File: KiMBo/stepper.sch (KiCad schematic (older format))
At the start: 18 parts

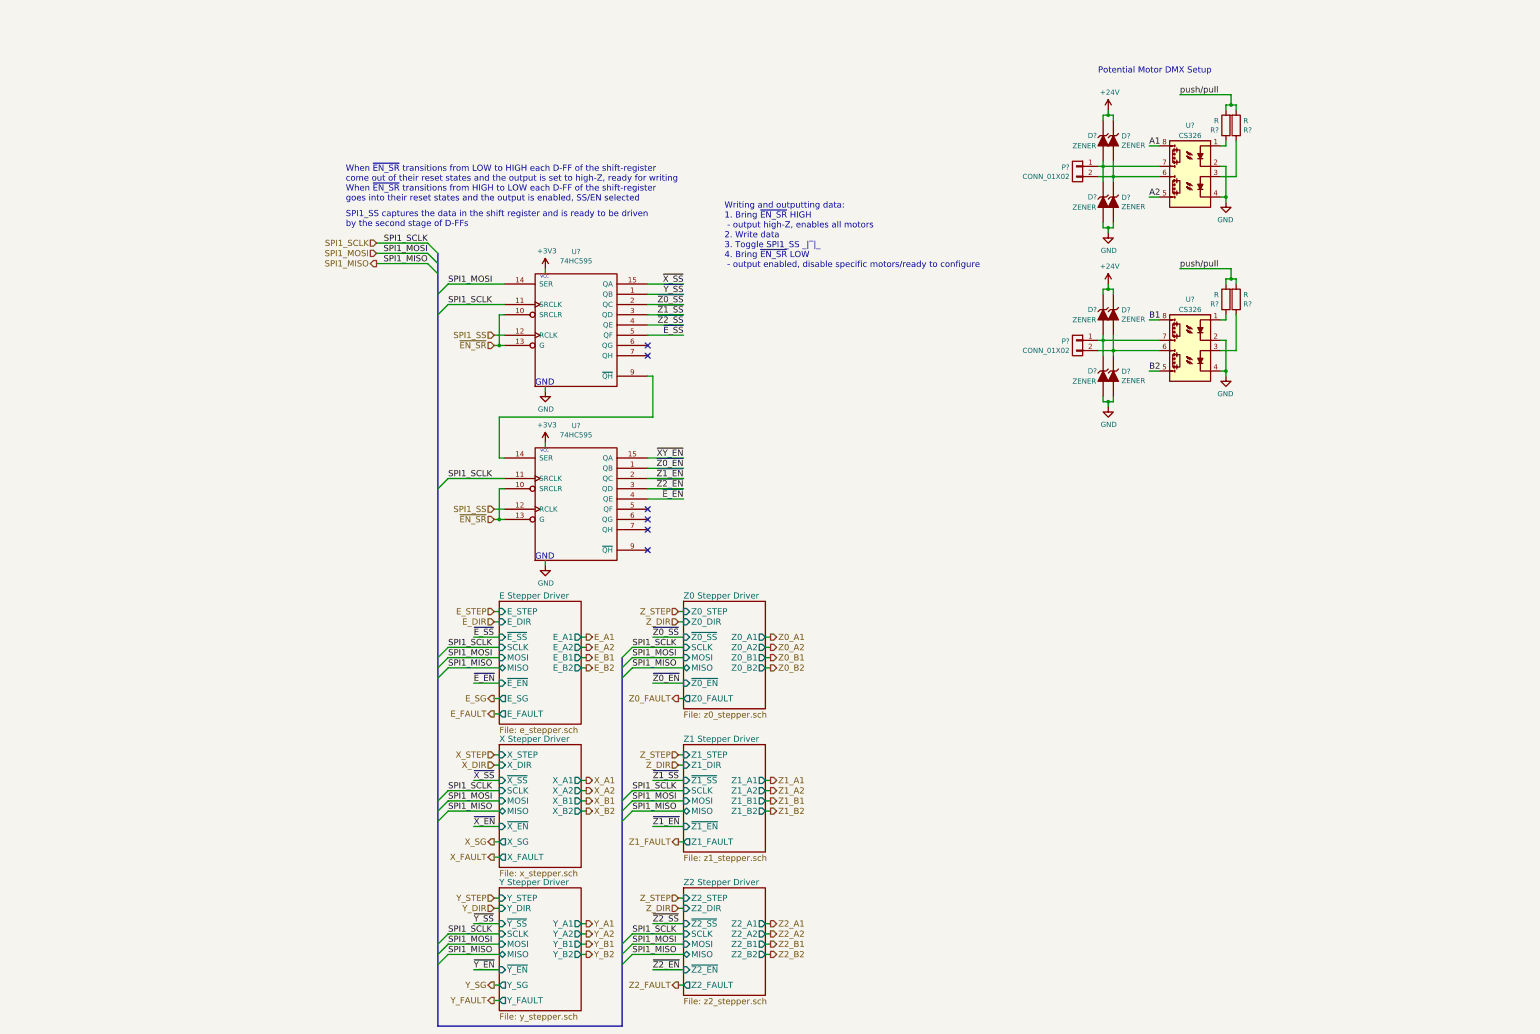
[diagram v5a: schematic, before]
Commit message: Create nodes for more SS, add H stepper, begin fixing power rail names
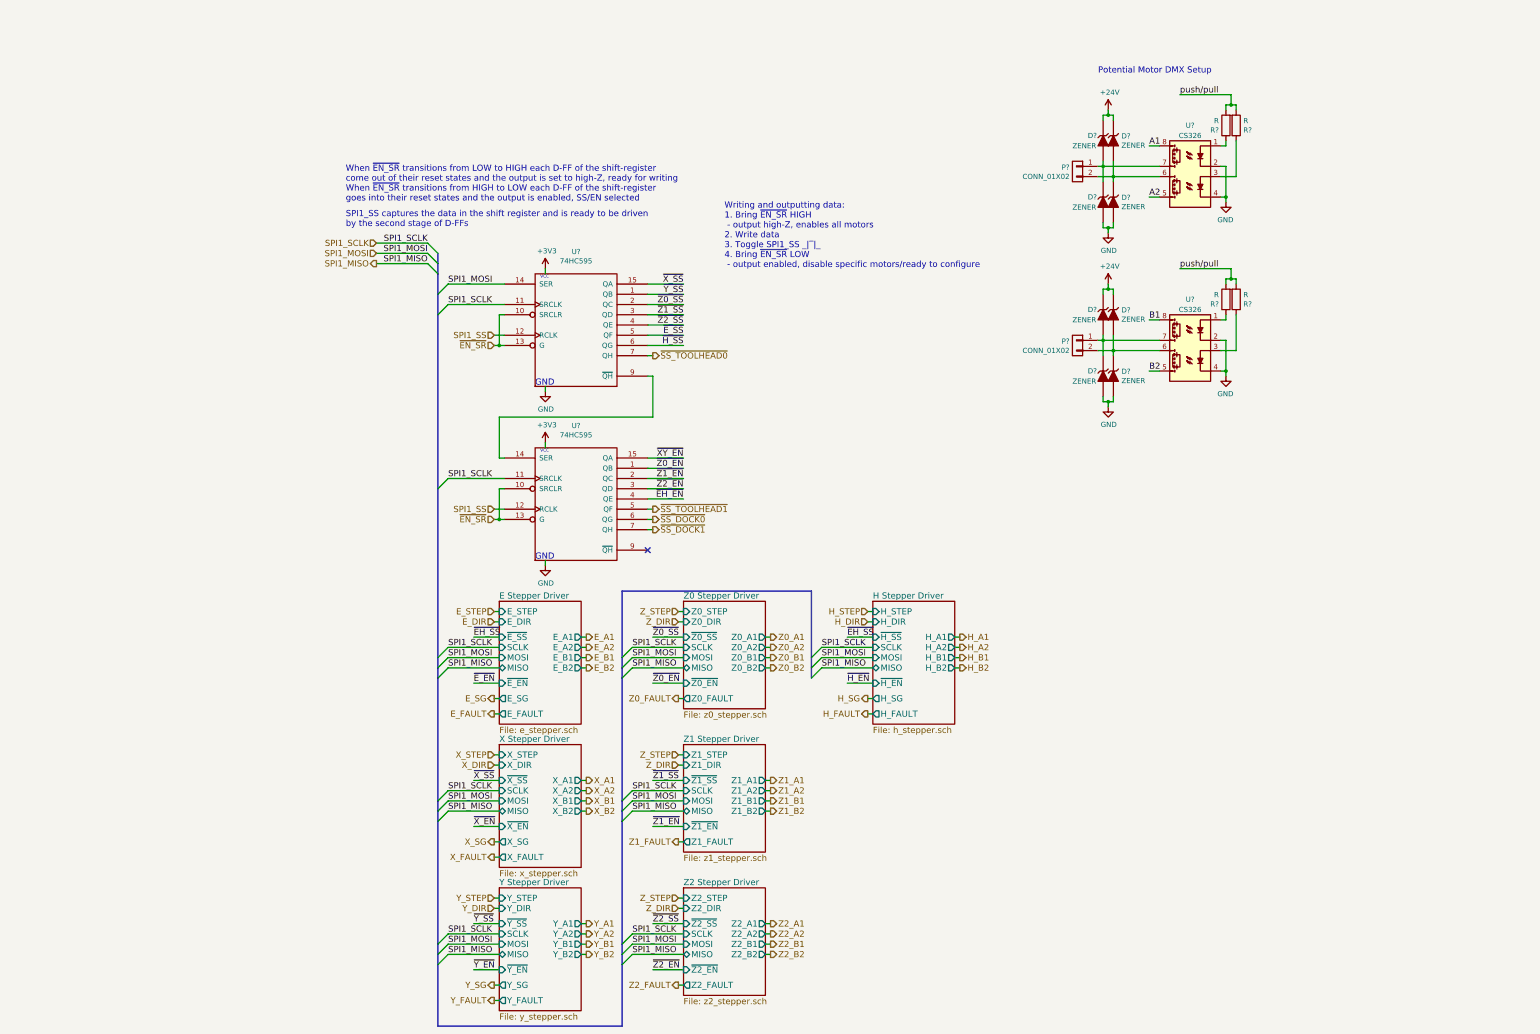
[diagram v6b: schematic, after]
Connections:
- net ~E_EN: no longer U?.4 (QE)
- net ~H_SS: now reaches U?.6 (QG)
- net ~SS_TOOLHEAD0: now reaches U?.7 (QH)
- net ~SS_TOOLHEAD1: now reaches U?.5 (QF)
- net ~SS_DOCK0: now reaches U?.6 (QG)
- net ~SS_DOCK1: now reaches U?.7 (QH)
- new net ~EH_EN: U?.4 (QE)
- no-connect marks 6 -> 1
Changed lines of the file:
@@
 $Descr A3 16535 11693
 encoding utf-8
-Sheet 16 23
+Sheet 10 25
 Title ""
 Date ""
@@
 ~Z2_SS
 Text Label 7200 5350 2    60   ~ 0
-~E_EN
+~EH_EN
 Text Label 7200 4950 2    60   ~ 0
 ~XY_EN
@@
 VCC
 Text Label 5150 6700 0    60   ~ 0
-~E_SS
+~EH_SS
 Text HLabel 5350 3850 0    60   Input ~ 0
 ~EN_SR
@@
 	4900 3450 5450 3450
 Wire Wire Line
-	5350 3850 5450 3850
+	5350 3850 5400 3850
+Wire Wire Line
+	5400 3850 5450 3850
 Wire Wire Line
 	5450 3750 5350 3750
@@
 Connection ~ 11400 3900
 Wire Wire Line
-	11400 3750 11400 3950
+	11400 3750 11400 3900
+Wire Wire Line
+	11400 3900 11400 3950
 Connection ~ 11300 3800
 Wire Wire Line
-	11300 3750 11300 3950
+	11300 3750 11300 3800
+Wire Wire Line
+	11300 3800 11300 3950
 Connection ~ 11350 4400
 Wire Wire Line
 	11350 4450 11350 4400
 Wire Wire Line
-	11300 4400 11400 4400
+	11300 4400 11350 4400
+Wire Wire Line
+	11350 4400 11400 4400
 Wire Wire Line
 	11400 4400 11400 4350
@@
 	11350 3300 11350 3250
 Wire Wire Line
-	11300 3300 11400 3300
+	11300 3300 11350 3300
+Wire Wire Line
+	11350 3300 11400 3300
 Wire Wire Line
 	11400 3300 11400 3350
@@
 	11850 3600 11750 3600
 Wire Wire Line
-	11250 3800 11850 3800
-Wire Wire Line
-	11250 3900 11850 3900
+	11250 3800 11300 3800
+Wire Wire Line
+	11300 3800 11850 3800
+Wire Wire Line
+	11250 3900 11400 3900
+Wire Wire Line
+	11400 3900 11850 3900
 Wire Wire Line
 	12550 3100 12050 3100
@@
 Connection ~ 12550 3200
 Wire Wire Line
-	12500 3200 12600 3200
+	12500 3200 12550 3200
+Wire Wire Line
+	12550 3200 12600 3200
 Wire Wire Line
 	12600 3200 12600 3250
@@
 	12500 3200 12500 3250
 Wire Wire Line
-	12500 3800 12500 4150
+	12500 3800 12500 4100
+Wire Wire Line
+	12500 4100 12500 4150
 Wire Wire Line
 	12450 4100 12500 4100
@@
 Connection ~ 11400 2200
 Wire Wire Line
-	11400 2050 11400 2250
+	11400 2050 11400 2200
+Wire Wire Line
+	11400 2200 11400 2250
 Connection ~ 11300 2100
 Wire Wire Line
-	11300 2050 11300 2250
+	11300 2050 11300 2100
+Wire Wire Line
+	11300 2100 11300 2250
 Connection ~ 11350 2700
 Wire Wire Line
 	11350 2750 11350 2700
 Wire Wire Line
-	11300 2700 11400 2700
+	11300 2700 11350 2700
+Wire Wire Line
+	11350 2700 11400 2700
 Wire Wire Line
 	11400 2700 11400 2650
@@
 	11350 1600 11350 1550
 Wire Wire Line
-	11300 1600 11400 1600
+	11300 1600 11350 1600
+Wire Wire Line
+	11350 1600 11400 1600
 Wire Wire Line
 	11400 1600 11400 1650
@@
 	11850 1900 11750 1900
 Wire Wire Line
-	11250 2100 11850 2100
-Wire Wire Line
-	11250 2200 11850 2200
+	11250 2100 11300 2100
+Wire Wire Line
+	11300 2100 11850 2100
+Wire Wire Line
+	11250 2200 11400 2200
+Wire Wire Line
+	11400 2200 11850 2200
 Wire Wire Line
 	12550 1400 12050 1400
@@
 Connection ~ 12550 1500
 Wire Wire Line
-	12500 1500 12600 1500
+	12500 1500 12550 1500
+Wire Wire Line
+	12550 1500 12600 1500
 Wire Wire Line
 	12600 1500 12600 1550
@@
 	12500 1500 12500 1550
 Wire Wire Line
-	12500 2100 12500 2450
+	12500 2100 12500 2400
+Wire Wire Line
+	12500 2400 12500 2450
 Wire Wire Line
 	12450 2400 12500 2400
@@
 	5400 6450 5350 6450
 Wire Bus Line
-	4800 2950 4800 10500
+	4800 2950 4800 3050
+Wire Bus Line
+	4800 3050 4800 3150
+Wire Bus Line
+	4800 3150 4800 3350
+Wire Bus Line
+	4800 3350 4800 3550
+Wire Bus Line
+	4800 3550 4800 5250
+Wire Bus Line
+	4800 5250 4800 6900
+Wire Bus Line
+	4800 6900 4800 7000
+Wire Bus Line
+	4800 7000 4800 7100
+Wire Bus Line
+	4800 7100 4800 8300
+Wire Bus Line
+	4800 8300 4800 8400
+Wire Bus Line
+	4800 8400 4800 8500
+Wire Bus Line
+	4800 8500 4800 9700
+Wire Bus Line
+	4800 9700 4800 9800
+Wire Bus Line
+	4800 9800 4800 9900
+Wire Bus Line
+	4800 9900 4800 10500
 Wire Wire Line
 	4900 7000 5400 7000
@@
 	4900 6800 5400 6800
 Wire Bus Line
-	6600 6900 6600 10500
+	6600 6250 6600 6900
+Wire Bus Line
+	6600 6900 6600 7000
+Wire Bus Line
+	6600 7000 6600 7100
+Wire Bus Line
+	6600 7100 6600 8300
+Wire Bus Line
+	6600 8300 6600 8400
+Wire Bus Line
+	6600 8400 6600 8500
+Wire Bus Line
+	6600 8500 6600 9700
+Wire Bus Line
+	6600 9700 6600 9800
+Wire Bus Line
+	6600 9800 6600 9900
+Wire Bus Line
+	6600 9900 6600 10500
 Wire Bus Line
 	6600 10500 4800 10500
@@
 	4900 5150 5450 5150
 Wire Wire Line
-	5350 5550 5450 5550
+	5350 5550 5400 5550
+Wire Wire Line
+	5400 5550 5450 5550
 Wire Wire Line
 	5450 5450 5350 5450
@@
 Text Label 7200 5250 2    60   ~ 0
 ~Z2_EN
-NoConn ~ 6850 5450
-NoConn ~ 6850 5550
-NoConn ~ 6850 5650
-NoConn ~ 6850 3850
 Wire Wire Line
 	5450 4950 5400 4950
@@
 Text Notes 7600 3100 0    60   ~ 0
 Writing and outputting data:\n1. Bring ~EN_SR~ HIGH\n - output high-Z, enables all motors\n2. Write data\n3. Toggle SPI1_SS _|‾|_\n4. Bring ~EN_SR~ LOW\n - output enabled, disable specific motors/ready to configure
-NoConn ~ 6850 3950
 Entry Wire Line
 	4900 5150 4800 5250
@@
 F13 "~Z2_EN" I L 7200 9950 60
 $EndSheet
+$Sheet
+S 9050 6350 800  1200
+U 59A0BA3D
+F0 "H Stepper Driver" 60
+F1 "h_stepper.sch" 60
+F2 "SCLK" I L 9050 6800 60
+F3 "MISO" T L 9050 7000 60
+F4 "MOSI" I L 9050 6900 60
+F5 "H_A1" O R 9850 6700 60
+F6 "H_A2" O R 9850 6800 60
+F7 "H_B1" O R 9850 6900 60
+F8 "H_B2" O R 9850 7000 60
+F9 "H_STEP" I L 9050 6450 60
+F10 "H_DIR" I L 9050 6550 60
+F11 "~H_SS" I L 9050 6700 60
+F12 "~H_EN" I L 9050 7150 60
+F13 "H_SG" O L 9050 7300 60
+F14 "H_FAULT" O L 9050 7450 60
+$EndSheet
+Entry Wire Line
+	8550 7000 8450 7100
+Entry Wire Line
+	8550 6900 8450 7000
+Text HLabel 9000 6450 0    60   Input ~ 0
+H_STEP
+Text HLabel 9000 6550 0    60   Input ~ 0
+H_DIR
+Text HLabel 9000 7300 0    60   Output ~ 0
+H_SG
+Text Label 8800 6700 0    60   ~ 0
+~EH_SS
+Text Label 8800 7150 0    60   ~ 0
+~H_EN
+Entry Wire Line
+	8550 6800 8450 6900
+Text Label 8550 6900 0    60   ~ 0
+SPI1_MOSI
+Text Label 8550 6800 0    60   ~ 0
+SPI1_SCLK
+Text Label 8550 7000 0    60   ~ 0
+SPI1_MISO
+Wire Wire Line
+	9050 7300 9000 7300
+Wire Wire Line
+	9050 7150 8800 7150
+Wire Wire Line
+	9050 6700 8800 6700
+Wire Wire Line
+	9050 6550 9000 6550
+Wire Wire Line
+	9050 6450 9000 6450
+Wire Wire Line
+	8550 7000 9050 7000
+Wire Wire Line
+	8550 6900 9050 6900
+Wire Wire Line
+	8550 6800 9050 6800
+Wire Wire Line
+	9850 6700 9900 6700
+Wire Wire Line
+	9850 6800 9900 6800
+Wire Wire Line
+	9850 6900 9900 6900
+Wire Wire Line
+	9850 7000 9900 7000
+Text HLabel 9000 7450 0    60   Output ~ 0
+H_FAULT
+Wire Wire Line
+	9050 7450 9000 7450
+Text HLabel 9900 6700 2    60   Output ~ 0
+H_A1
+Text HLabel 9900 6800 2    60   Output ~ 0
+H_A2
+Text HLabel 9900 6900 2    60   Output ~ 0
+H_B1
+Text HLabel 9900 7000 2    60   Output ~ 0
+H_B2
+Wire Bus Line
+	8450 6250 8450 6900
+Wire Bus Line
+	8450 6900 8450 7000
+Wire Bus Line
+	8450 7000 8450 7100
+Wire Bus Line
+	8450 6250 6600 6250
+Wire Wire Line
+	6850 5450 6900 5450
+Wire Wire Line
+	6850 3850 7200 3850
+Text Label 7200 3850 2    60   ~ 0
+~H_SS
+Text HLabel 6900 3950 2    60   Output ~ 0
+~SS_TOOLHEAD0
+Wire Wire Line
+	6850 3950 6900 3950
+Text HLabel 6900 5550 2    60   Output ~ 0
+~SS_DOCK0
+Text HLabel 6900 5650 2    60   Output ~ 0
+~SS_DOCK1
+Wire Wire Line
+	6850 5550 6900 5550
+Wire Wire Line
+	6850 5650 6900 5650
+Text HLabel 6900 5450 2    60   Output ~ 0
+~SS_TOOLHEAD1
 $EndSCHEMATC

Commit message: Update the rest of the power rails and add two more stepper drivers
Now has *nine* stepper drivers, this will increase cost, and may drastically increase development time...
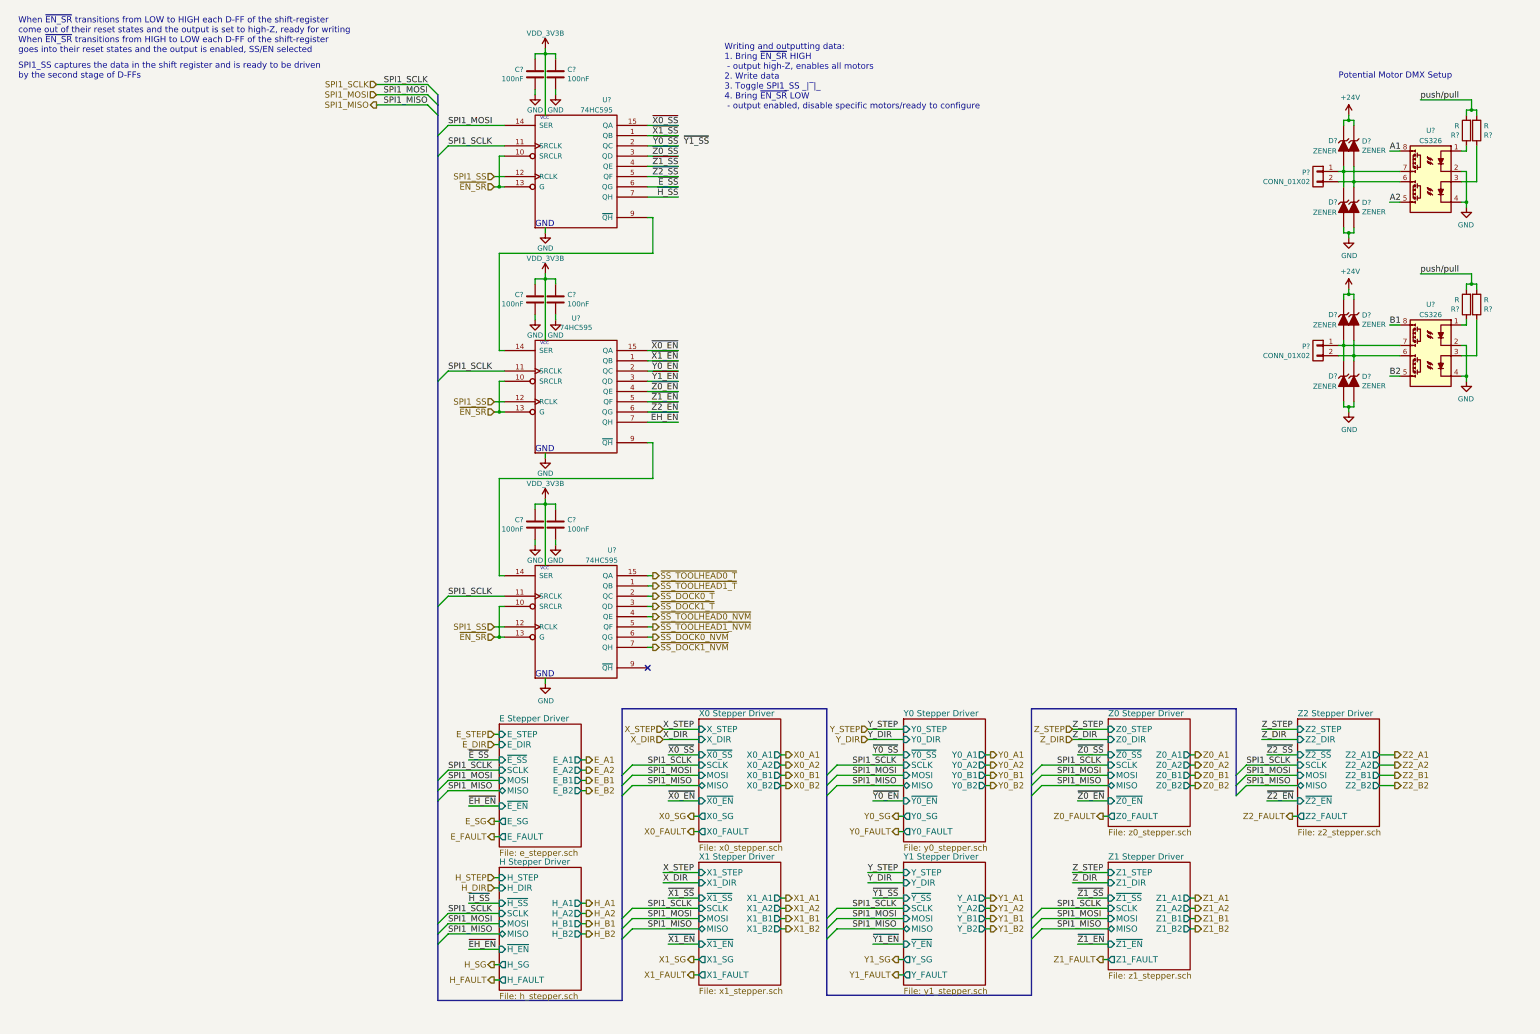
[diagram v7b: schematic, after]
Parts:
- added C? (x6): 100nF, symbol C
- added U?: 74HC595, symbol 74HC595
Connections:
- net ~SS_DOCK0 is gone; now on net ~Z2_EN: U?.6 (QG)
- net ~SS_DOCK1 is gone; now on net ~EH_EN: U?.7 (QH)
- net ~SS_TOOLHEAD0 is gone; now on net ~H_SS: U?.7 (QH)
- net ~SS_TOOLHEAD1 is gone; now on net ~Z1_EN: U?.5 (QF)
- net GND: now also C?.1, C?.2, C?.2, C?.2, C?.2, C?.2, U?.8 (GND)
- net SPI1_SCLK: now also U?.11 (SRCLK)
- net SPI1_SS: now also U?.12 (RCLK)
- net ~EH_EN: no longer U?.4 (QE)
- net ~EN_SR: now also U?.10 (SRCLR), U?.13 (G)
- net ~E_SS: now also U?.6 (QG); no longer U?.5 (QF)
- net ~H_SS: no longer U?.6 (QG)
- net ~Z0_EN: now also U?.4 (QE); no longer U?.1 (QB)
- net ~Z0_SS: now also U?.3 (QD); no longer U?.2 (QC)
- net ~Z1_EN: no longer U?.2 (QC)
- net ~Z1_SS: now also U?.4 (QE); no longer U?.3 (QD)
- net ~Z2_EN: no longer U?.3 (QD)
- net ~Z2_SS: now also U?.5 (QF); no longer U?.4 (QE)
- net at U?.9 (~QH): now also U?.14 (SER)
- net +3V3 renamed VCC
- net VCC: now also C?.1, C?.1, C?.1, C?.1, C?.1, C?.2, U?.16 (VCC)
- net ~XY_EN renamed ~X0_EN
- net ~X_SS renamed ~X0_SS
- net ~Y_SS renamed ~X1_SS
- new net ~SS_DOCK0_NVM: U?.6 (QG)
- new net ~SS_DOCK0_T: U?.2 (QC)
- new net ~SS_DOCK1_NVM: U?.7 (QH)
- new net ~SS_DOCK1_T: U?.3 (QD)
- new net ~SS_TOOLHEAD0_NVM: U?.4 (QE)
- new net ~SS_TOOLHEAD0_T: U?.15 (QA)
- new net ~SS_TOOLHEAD1_NVM: U?.5 (QF)
- new net ~SS_TOOLHEAD1_T: U?.1 (QB)
- new net ~X1_EN: U?.1 (QB)
- new net ~Y0_EN: U?.2 (QC)
- new net ~Y0_SS: U?.2 (QC)
- new net ~Y1_EN: U?.3 (QD)
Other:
- moved on the sheet: D?, P?, R?, U?
